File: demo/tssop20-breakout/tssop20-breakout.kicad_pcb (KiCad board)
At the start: 2 copper layers, 17.8 x 25.4 mm, 5 parts, among them J1 Conn_01x10, J2 Conn_01x10, U1 CH32V30xFxPx

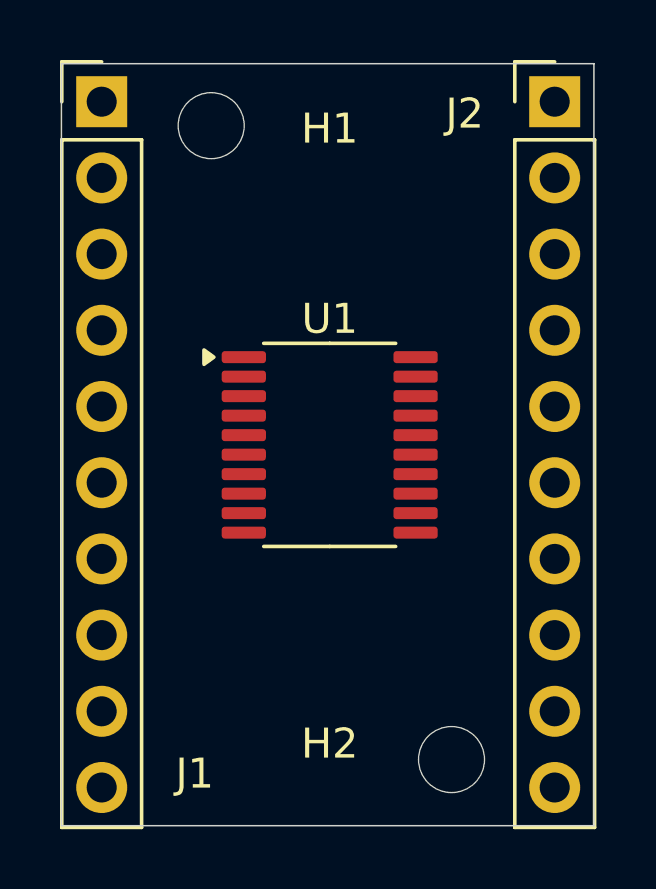
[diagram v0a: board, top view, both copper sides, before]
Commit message: Better alignment of chip footprint in breakout
Chip is moved lower by 0.325 mm. Determined empirically by printing
a jig. Last leg was between pads. So moved down by gap between pads
plus half of extra width of the pad.
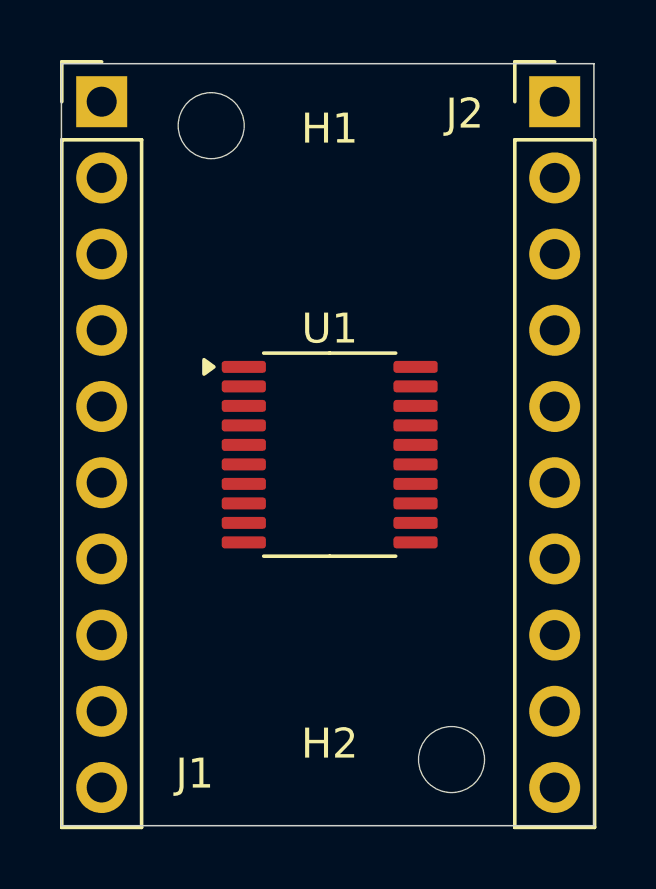
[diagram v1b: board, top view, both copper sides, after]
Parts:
- moved U1 0.32 mm to (114.0, 117.4)
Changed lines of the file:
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@@
 	(footprint "Package_SO:TSSOP-20_4.4x6.5mm_P0.65mm"
 		(layer "F.Cu")
-		(at 114 117.04)
+		(at 114 117.365)
 		(descr "TSSOP, 20 Pin (JEDEC MO-153 Var AC https://www.jedec.org/document_search?search_api_views_fulltext=MO-153), generated with kicad-footprint-generator ipc_gullwing_generator.py")
 		(tags "TSSOP SO")
